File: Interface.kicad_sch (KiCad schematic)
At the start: 37 parts, among them SW1 SW_Push, SW2 SW_Push, SW3 SW_Push, SW4 SW_Push, SW5 SW_Push, SW6 SW_Push

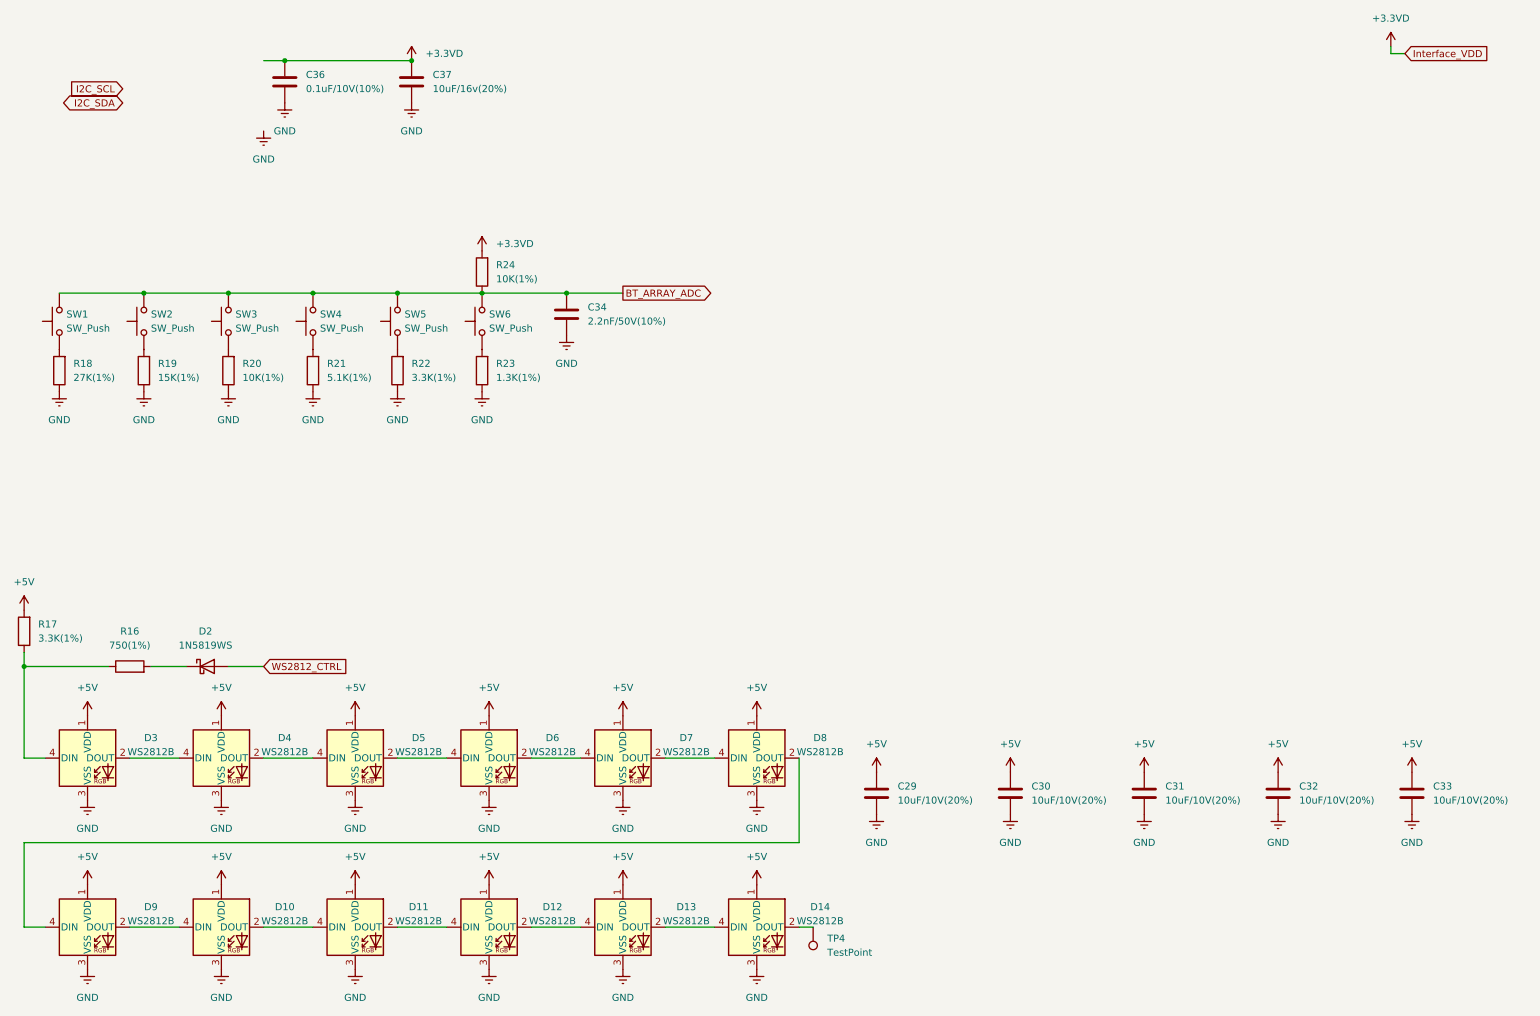
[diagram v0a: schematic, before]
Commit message: Initial population of PCB
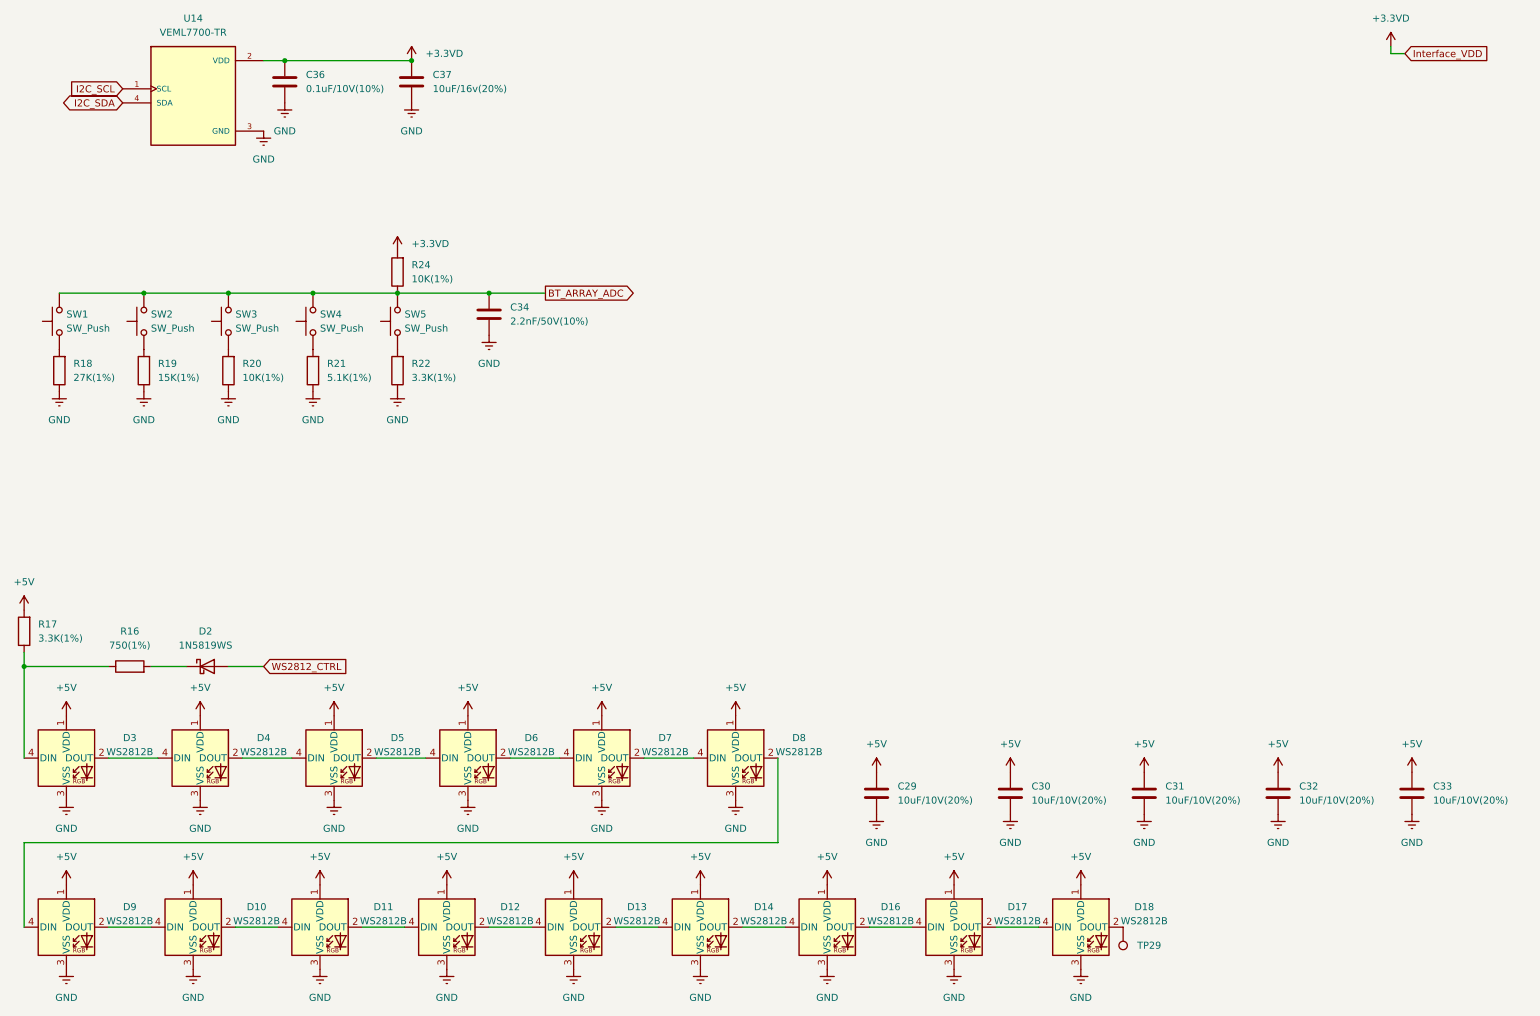
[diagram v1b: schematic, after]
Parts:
- removed R23: 1.3K(1%), Resistor_SMD:R_0603_1608Metric, symbol Device:R
- removed SW6: SW_Push, symbol Switch:SW_Push
- removed TP4: TestPoint, TestPoint:TestPoint_Pad_D1.5mm, symbol Connector:TestPoint
- added D16, D17, D18: WS2812B, LED_SMD:LED_WS2812B_PLCC4_5.0x5.0mm_P3.2mm, symbol LED:WS2812B
- added TP29: TestPoint, TestPoint:TestPoint_Pad_D1.5mm, symbol Connector:TestPoint
- added U14: VEML7700-TR, Library:XDCR_VEML7700-TR, symbol VEML7700-TR:VEML7700-TR
- SW1, SW2, SW3, SW4, SW5: footprint (none) -> Button_Switch_SMD:SW_SPST_PTS645
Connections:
- net +3.3VD: now also U14.2 (VDD)
- net +5V: now also D16.1 (VDD), D17.1 (VDD), D18.1 (VDD)
- net GND: now also D16.3 (VSS), D17.3 (VSS), D18.3 (VSS), U14.3 (GND)
- net I2C_SCL: now also U14.1 (SCL)
- net I2C_SDA: now also U14.4 (SDA)
- net at D14.2 (DOUT): now also D16.4 (DIN)
- new net: D16.2 (DOUT), D17.4 (DIN)
- new net: D18.2 (DOUT), TP29.1
- new net: D17.2 (DOUT), D18.4 (DIN)
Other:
- moved on the sheet: C34, D10, D11, D12, D13, D14, D3, D4, D5, D6, D7, D8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

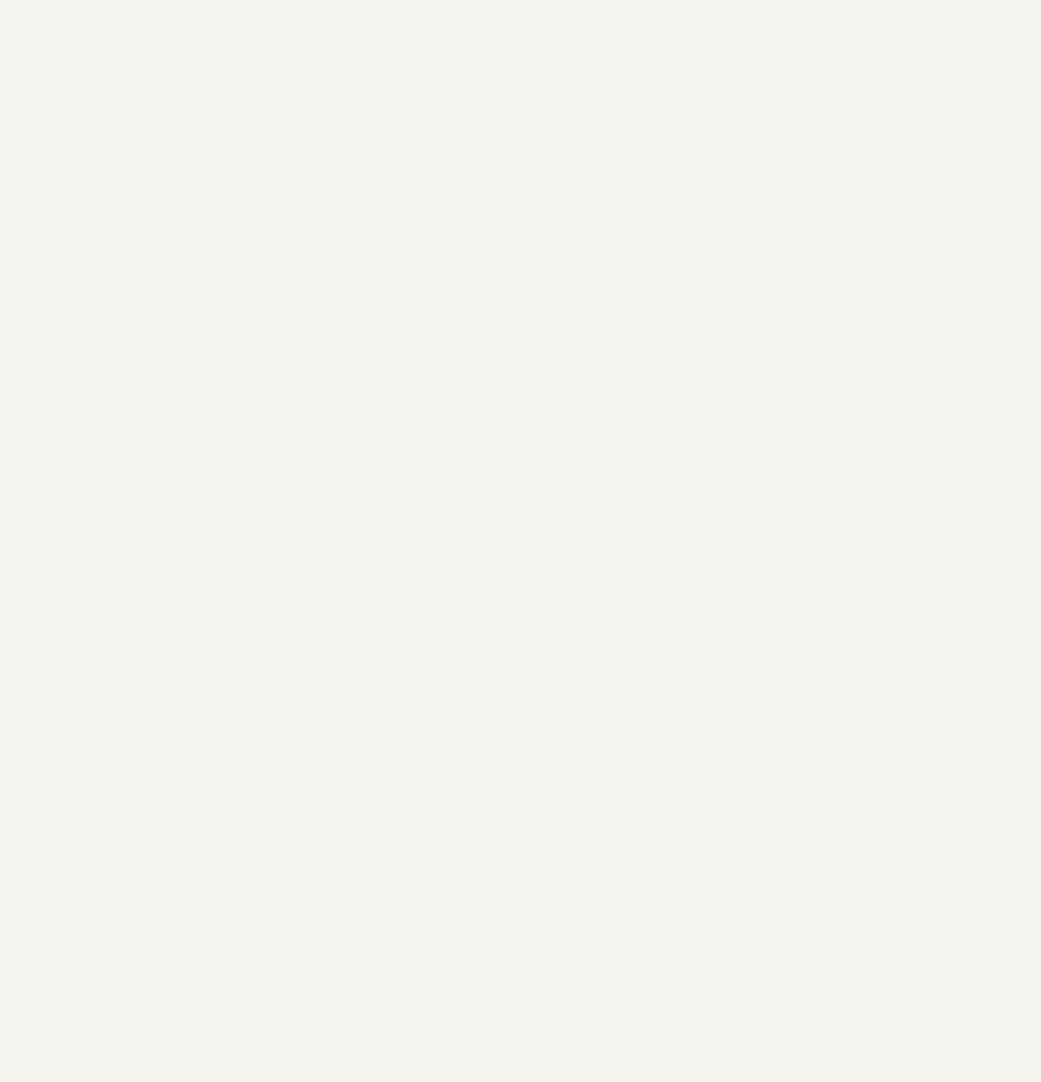
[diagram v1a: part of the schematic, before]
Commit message: Added DSP, Neopixles, MIC's and mounting holes
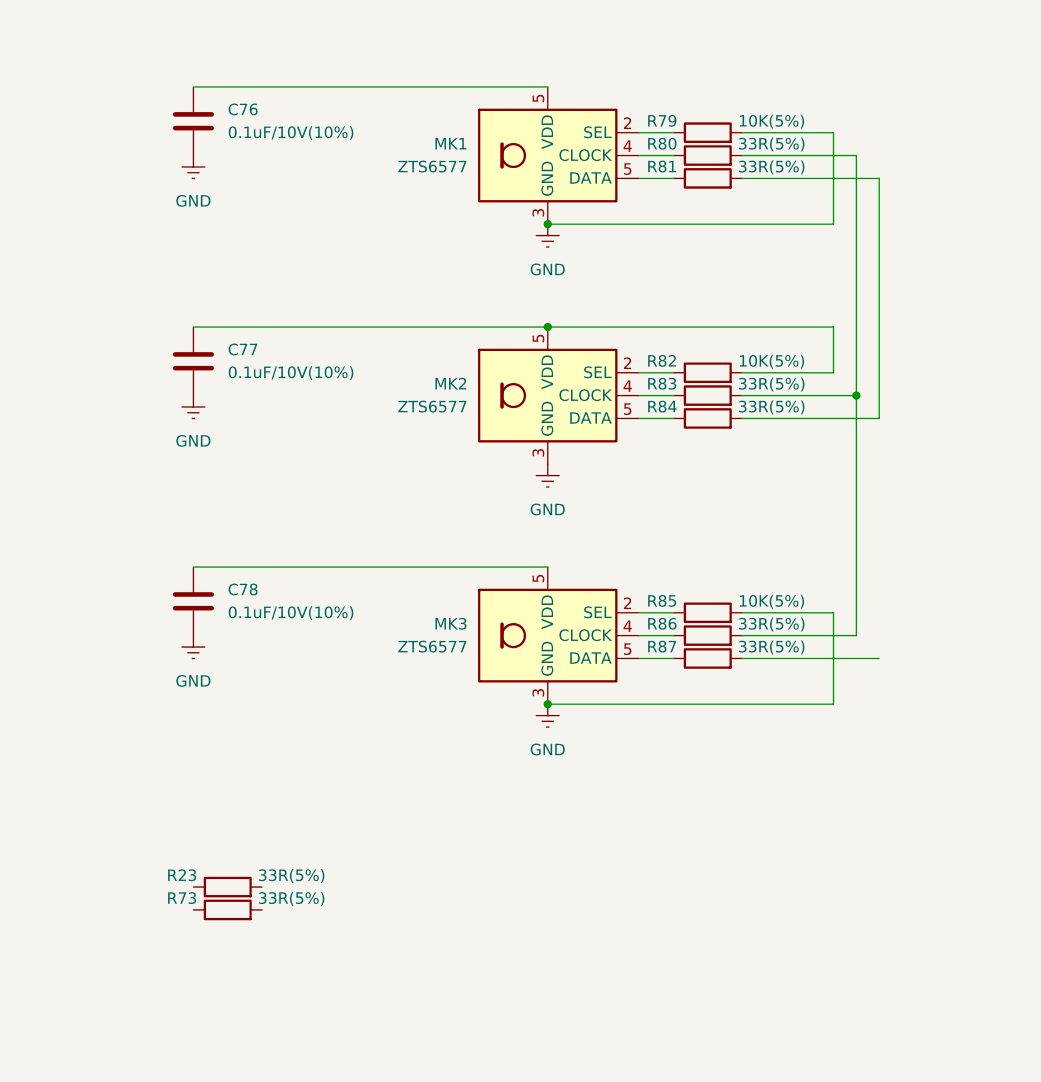
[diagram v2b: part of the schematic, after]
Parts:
- added C76, C77, C78: 0.1uF/10V(10%), Capacitor_SMD:C_0402_1005Metric, symbol Device:C
- added MK1, MK2, MK3: ZTS6577, Knowles_LGA-5_3.5x2.65mm:Knowles_LGA-5_3.5x2.65mm, symbol ZILLTEK ZTS6577:ZTS6577
- added R23, R73, R80, R81, R83, R84, R86, R87: 33R(5%), Resistor_SMD:R_0402_1005Metric, symbol Device:R
- added R79, R82, R85: 10K(5%), Resistor_SMD:R_0402_1005Metric, symbol Device:R
- C29, C30, C31, C32, C33, C34, C36, C37: footprint Capacitor_SMD:C_0603_1608Metric -> Capacitor_SMD:C_0402_1005Metric
- R16, R17, R18, R19, R20, R21, R22, R24: footprint Resistor_SMD:R_0603_1608Metric -> Resistor_SMD:R_0402_1005Metric
- TP29: footprint TestPoint:TestPoint_Pad_D1.5mm -> TestPoint:TestPoint_Pad_D1.0mm
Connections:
- net GND: now also C76.2, C77.2, C78.2, MK1.3 (GND), MK2.3 (GND), MK3.3 (GND), R79.2, R85.2
- new net: C78.1, MK3.5 (VDD)
- new net: C76.1, MK1.5 (VDD)
- new net: MK3.5 (VDD), R87.1
- new net: MK2.4 (CLOCK), R83.1
- new net: R80.2, R83.2, R86.2
- new net: MK1.2 (SEL), R79.1
- new net: MK2.2 (SEL), R82.1
- new net: C77.1, MK2.5 (VDD), R82.2
- new net: MK2.5 (VDD), R84.1
- new net: R81.2, R84.2
- new net: MK1.4 (CLOCK), R80.1
- new net: MK1.5 (VDD), R81.1
- new net: MK3.2 (SEL), R85.1
- new net: MK3.4 (CLOCK), R86.1
